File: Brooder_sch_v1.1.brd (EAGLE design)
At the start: 100 x 90 mm, 37 parts, among them J1 DCJ0202, J2 1X2-3.5MM, J3 DCJ0202, J4 1X2-3.5MM, T1 2N2222, U1 328P

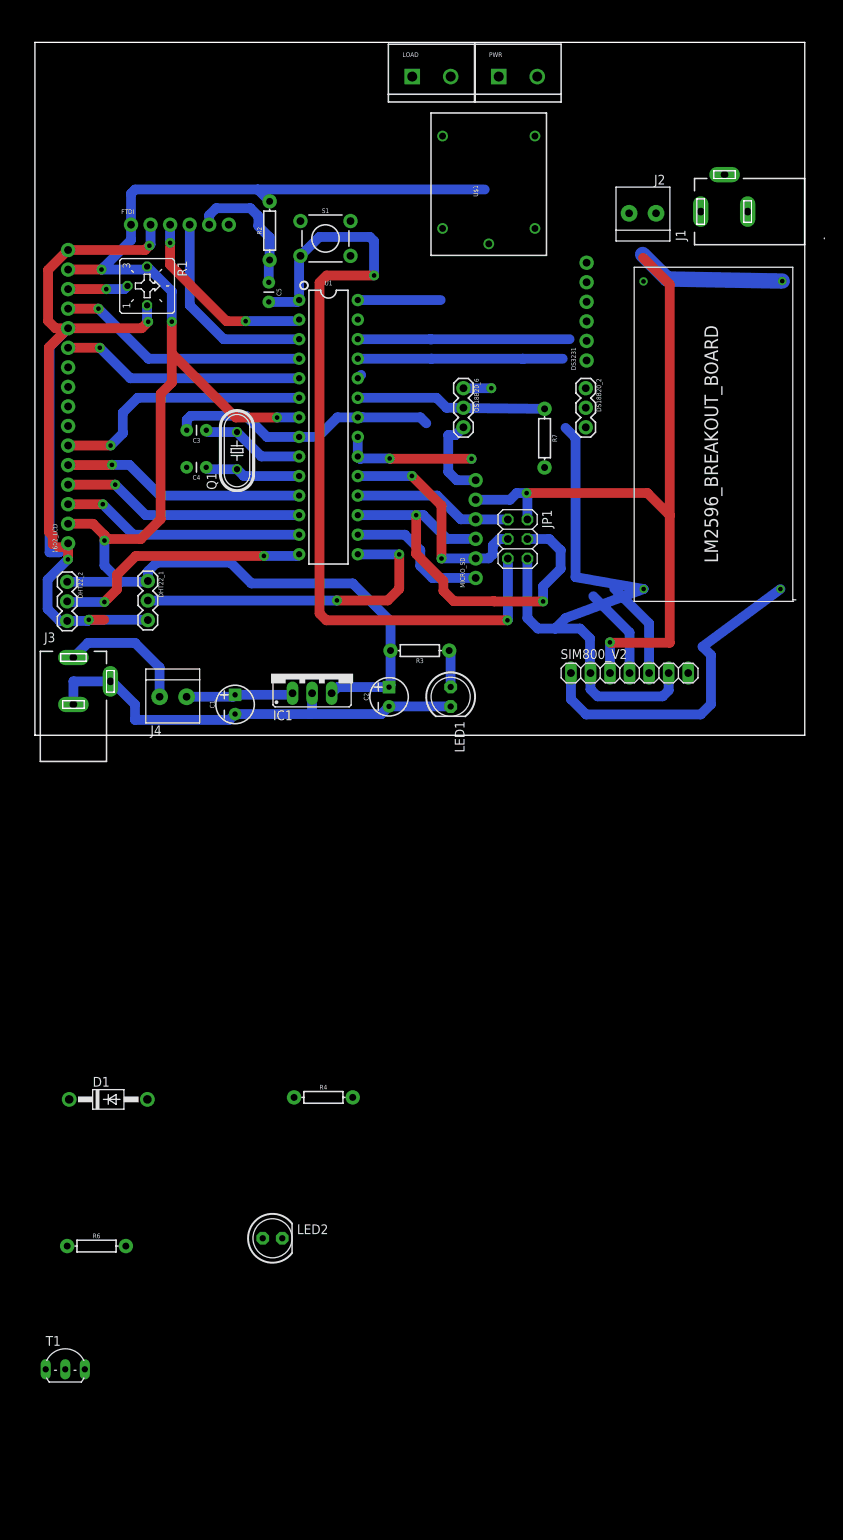
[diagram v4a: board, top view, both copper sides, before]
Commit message: Replaces both power jacks with header pins
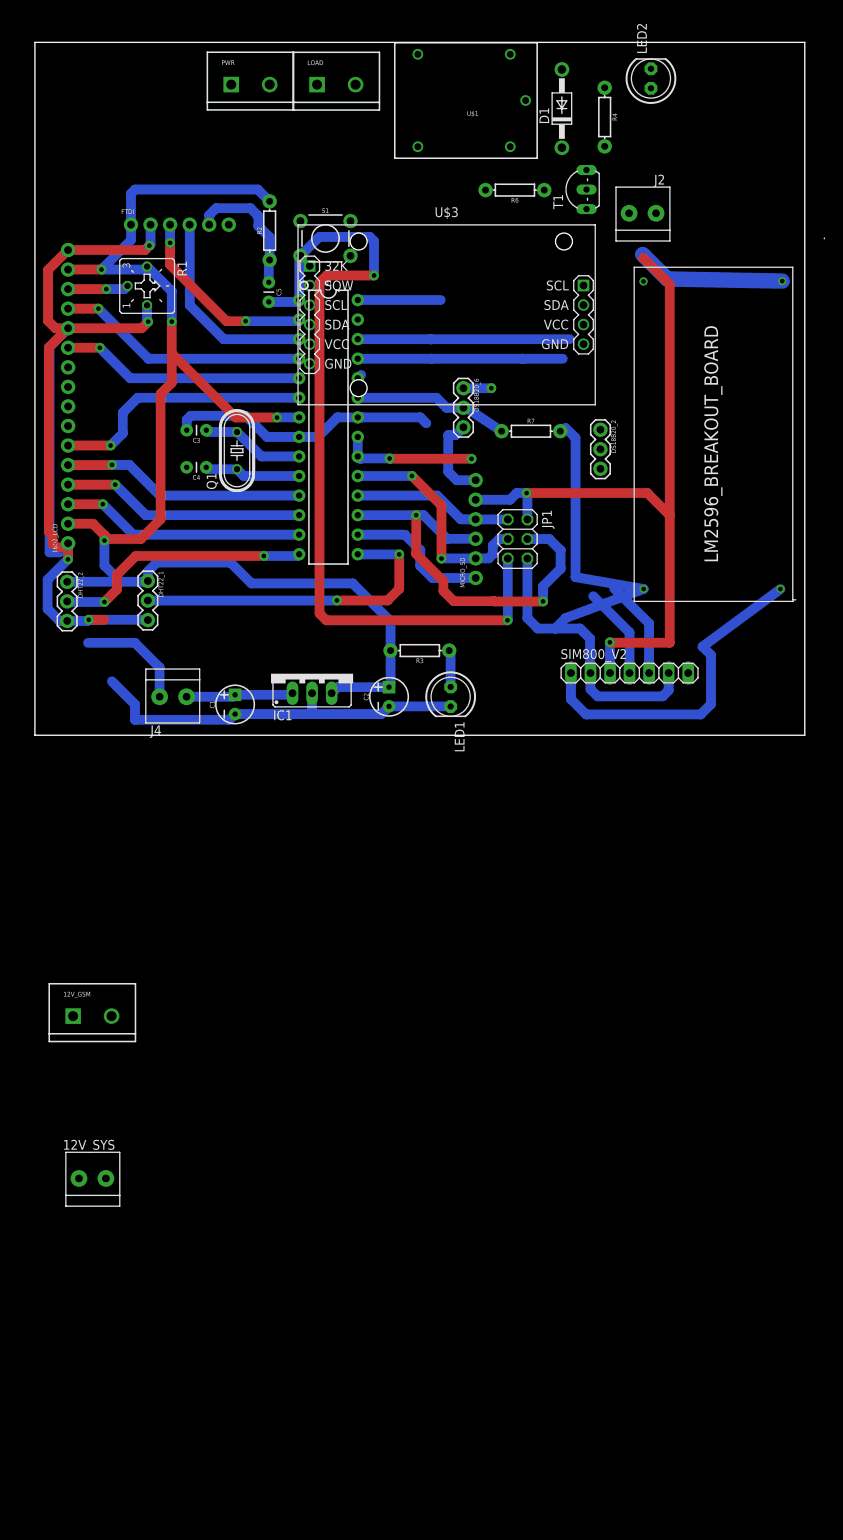
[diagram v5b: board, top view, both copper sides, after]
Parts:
- removed DS3231: (no value), SparkFun-Connectors:1X06_NO_SILK
- removed J1, J3: DCJ0202, con-jack:DCJ0202
- added 12V_GSM: (no value), SparkFun-Connectors:SCREWTERMINAL-5MM-2
- added 12V_SYS: 1X2-3.5MM, adafruit:1X2-3.5MM
- added U$3: RTC-DS3231-AT24C32, diy-modules-1.8.0:RTC-DS3231-AT24C32
- moved T1 165.9 mm to (70.4, 70.9), turned to 90 degrees
- moved LED2 158.5 mm to (80.0, 85.3), turned to 90 degrees
- moved R6 147.5 mm to (62.4, 70.8), turned to 180 degrees
- moved D1 141.5 mm to (68.5, 81.4), turned to 90 degrees
- moved R4 132.5 mm to (74.0, 80.3), turned to 270 degrees
- moved PWR 34.8 mm to (25.5, 84.5)
- moved LOAD 12.4 mm to (36.6, 84.5)
- moved U$1 11.4 mm to (56.4, 82.3), turned to 180 degrees
- moved DS18B20_2 5.72 mm to (73.5, 39.7)
- moved R7 1.99 mm to (64.4, 39.5), turned to 0 degrees
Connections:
- removed net PC4: DS3231.4, U1.27
- removed net PC5: DS3231.3, U1.28
- new net GND.1: U$3.J1.6
- new net SCL: U$3.J2.1, U1.28
- new net SDA: U$3.J2.2, U1.27
- new net VCC.1: U$3.J1.5
- net 12V: now also 12V_SYS.1; no longer J3.1
- net 12V_SIM: now also 12V_GSM.1; no longer J1.1
- net 5V: now also U$3.J2.3; no longer DS3231.5
- net GND: now also 12V_GSM.2, 12V_SYS.2, U$3.J2.4; no longer DS3231.6, J1.2, J1.3, J3.2, J3.3
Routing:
- net 5V: track 325.3 -> 295.8 mm
- net SCL: track 0.00 -> 10.8 mm
- net PC5: track 10.8 -> 0.00 mm
- net GND: track 313.0 -> 305.0 mm
- net PC0: track 24.8 -> 20.1 mm
- net 12V: track 17.1 -> 14.4 mm

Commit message: Adds custom sim800V2 library symbol to schematic
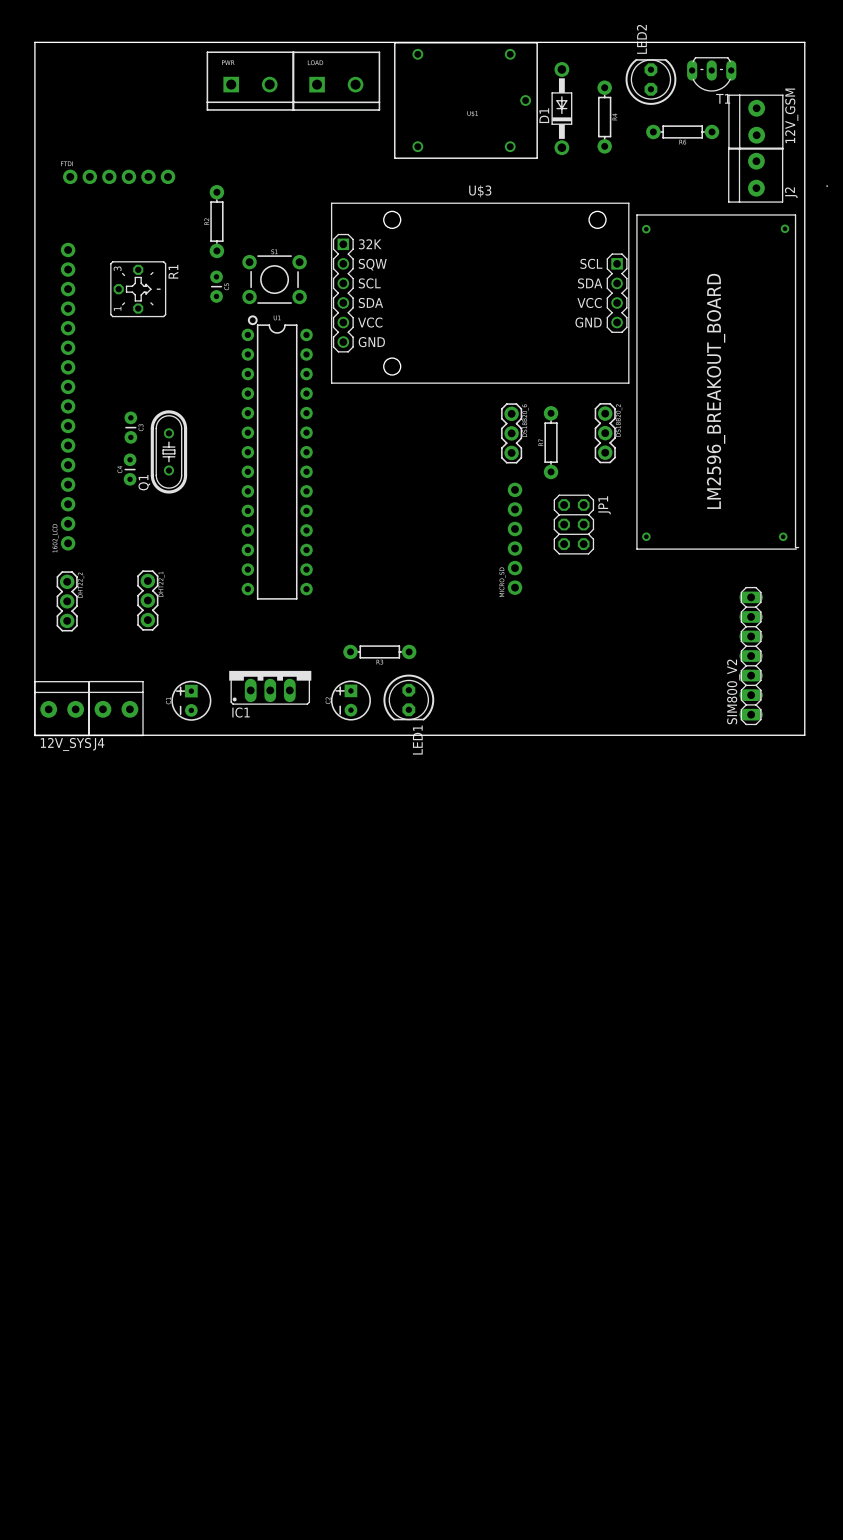
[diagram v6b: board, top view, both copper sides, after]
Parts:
- 12V_GSM: value (none) -> 1X2-3.5MM; device SparkFun-Connectors:SCREWTERMINAL-5MM-2 -> adafruit:1X2-3.5MM
- moved 12V_GSM 146.3 mm to (93.8, 79.7), turned to 270 degrees
- moved 12V_SYS 61.1 mm to (3.59, 3.36), turned to 180 degrees
- moved R6 23.1 mm to (84.1, 78.4)
- moved T1 22.6 mm to (87.9, 85.1), turned to 180 degrees
- moved SIM800_V2 15.9 mm to (93.0, 10.3), turned to 90 degrees
- moved J2 15.7 mm to (93.7, 72.9), turned to 270 degrees
- moved FTDI 10.0 mm to (4.59, 72.5)
- moved Q1 8.84 mm to (17.4, 36.8)
- moved C4 8.62 mm to (12.4, 34.5), turned to 90 degrees
- moved C3 8.54 mm to (12.5, 40.0), turned to 270 degrees
- moved S1 8.50 mm to (31.1, 59.2)
- moved U1 8.05 mm to (31.5, 35.5)
- moved JP1 7.55 mm to (70.0, 27.4)
- moved J4 7.54 mm to (10.6, 3.37)
- moved DS18B20_6 7.09 mm to (61.9, 41.8)
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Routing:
- net GND: track 305.0 -> 0.00 mm, vias 4 -> 0
- net 5V: track 295.8 -> 0.00 mm, vias 9 -> 0
- net RESET: track 108.6 -> 0.00 mm, vias 2 -> 0
- net MOSI: track 53.9 -> 0.00 mm, vias 2 -> 0
- net 5V_SIM: track 43.5 -> 0.00 mm
- net PB1: track 43.1 -> 0.00 mm, vias 2 -> 0
- net RX: track 40.5 -> 0.00 mm
- net TX: track 38.6 -> 0.00 mm
- net PD4: track 34.2 -> 0.00 mm, vias 1 -> 0
- net PB0: track 33.8 -> 0.00 mm, vias 2 -> 0
- net PD2: track 32.8 -> 0.00 mm, vias 1 -> 0
- net PD5: track 31.7 -> 0.00 mm, vias 1 -> 0
- net PD3: track 31.7 -> 0.00 mm, vias 1 -> 0
- net PD7: track 31.7 -> 0.00 mm, vias 1 -> 0
- net PD6: track 31.7 -> 0.00 mm, vias 1 -> 0
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
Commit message: Adds i2c header pin in place of lcd pins and potentiometer
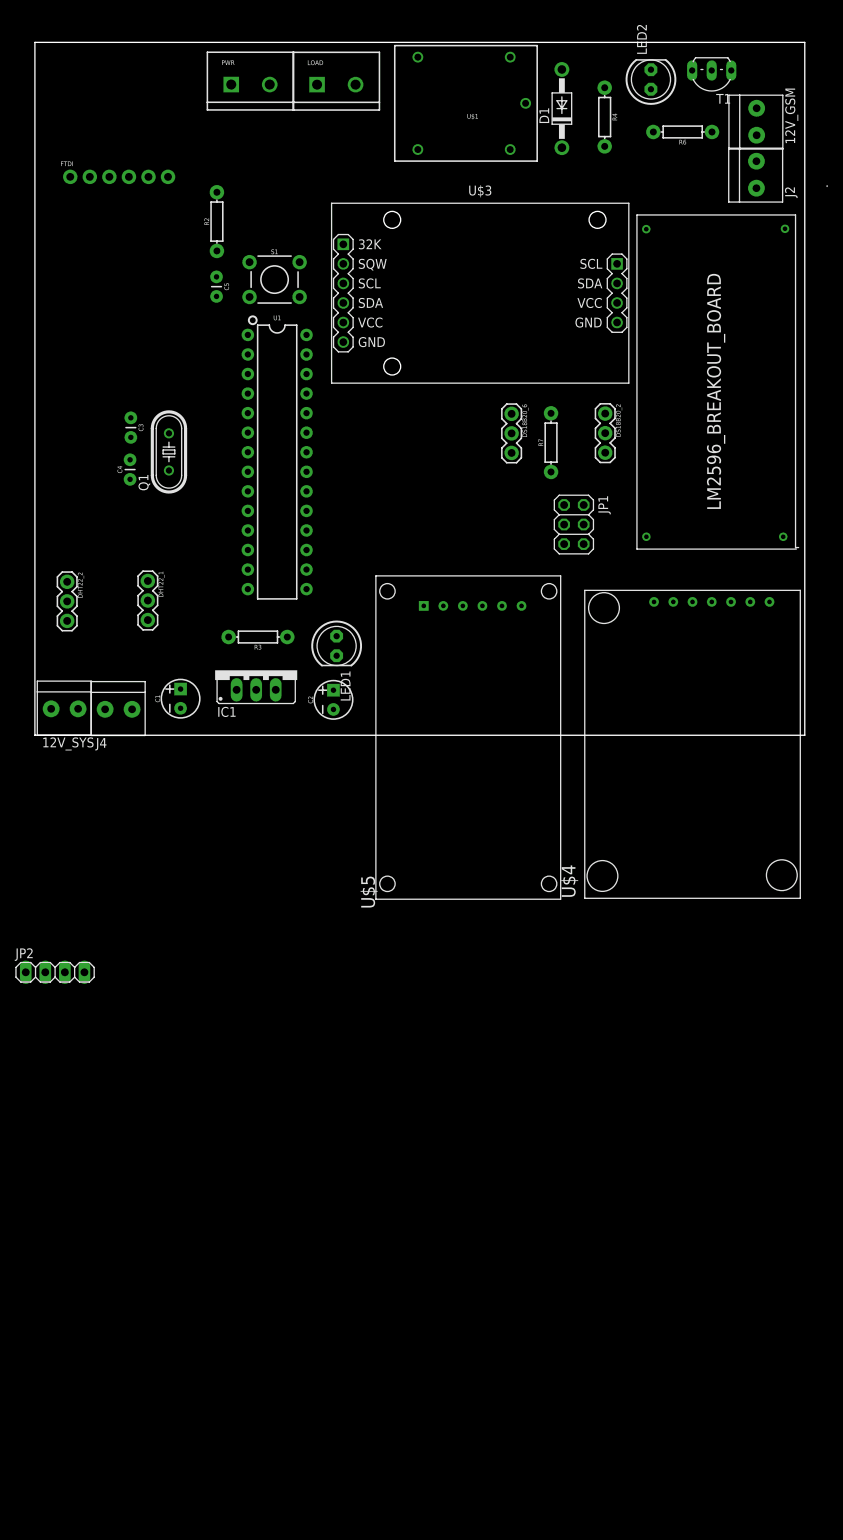
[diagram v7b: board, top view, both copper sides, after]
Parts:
- removed 1602_LCD: (no value), SparkFun-Connectors:1X16_NO_SILK
- removed MICRO_SD: (no value), SparkFun-Connectors:1X06_NO_SILK
- removed R1: (no value), pot:CT6
- removed SIM800_V2: (no value), pinhead:1X07
- added JP2: (no value), pinhead:1X04
- added U$4: (no value), custom_libraries:20*4_LCD
- added U$5: SD_CARD_MODULE, custom_libraries:SD_CARD_MODULE
- moved R3 15.9 mm to (29.0, 12.8)
- moved LED1 11.7 mm to (39.2, 11.6)
- moved C2 2.27 mm to (38.8, 4.60)
- moved IC1 1.83 mm to (28.7, 8.44)
- moved C1 1.43 mm to (18.9, 4.75)
- moved U$1 0.37 mm to (56.4, 82.0)
- moved 12V_SYS 0.33 mm to (3.91, 3.43)
- moved J4 0.28 mm to (10.9, 3.37)
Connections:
- removed net VO: 1602_LCD.14, R1.S
- net 5V: now also JP2.3, U$4.3, U$5.2; no longer 1602_LCD.15, 1602_LCD.2, MICRO_SD.5, R1.E, SIM800_V2.3
- net 5V_SIM: now also U$4.1; no longer SIM800_V2.1
- net GND: now also JP2.4, U$4.2, U$4.6, U$5.1; no longer 1602_LCD.1, 1602_LCD.12, 1602_LCD.16, MICRO_SD.6, R1.A, SIM800_V2.2, SIM800_V2.6
- net MISO: now also U$5.3; no longer MICRO_SD.4
- net MOSI: now also U$5.4; no longer MICRO_SD.3
- net PD2: no longer 1602_LCD.13
- net PD3: no longer 1602_LCD.11
- net PD4: no longer 1602_LCD.6
- net PD5: no longer 1602_LCD.5
- net PD6: no longer 1602_LCD.4
- net PD7: no longer 1602_LCD.3
- net RX: now also U$4.5; no longer SIM800_V2.5
- net SCK: now also U$5.5; no longer MICRO_SD.2
- net SCL: now also JP2.1
- net SDA: now also JP2.2
- net SS: now also U$5.6; no longer MICRO_SD.1
- net TX: now also U$4.4; no longer SIM800_V2.4

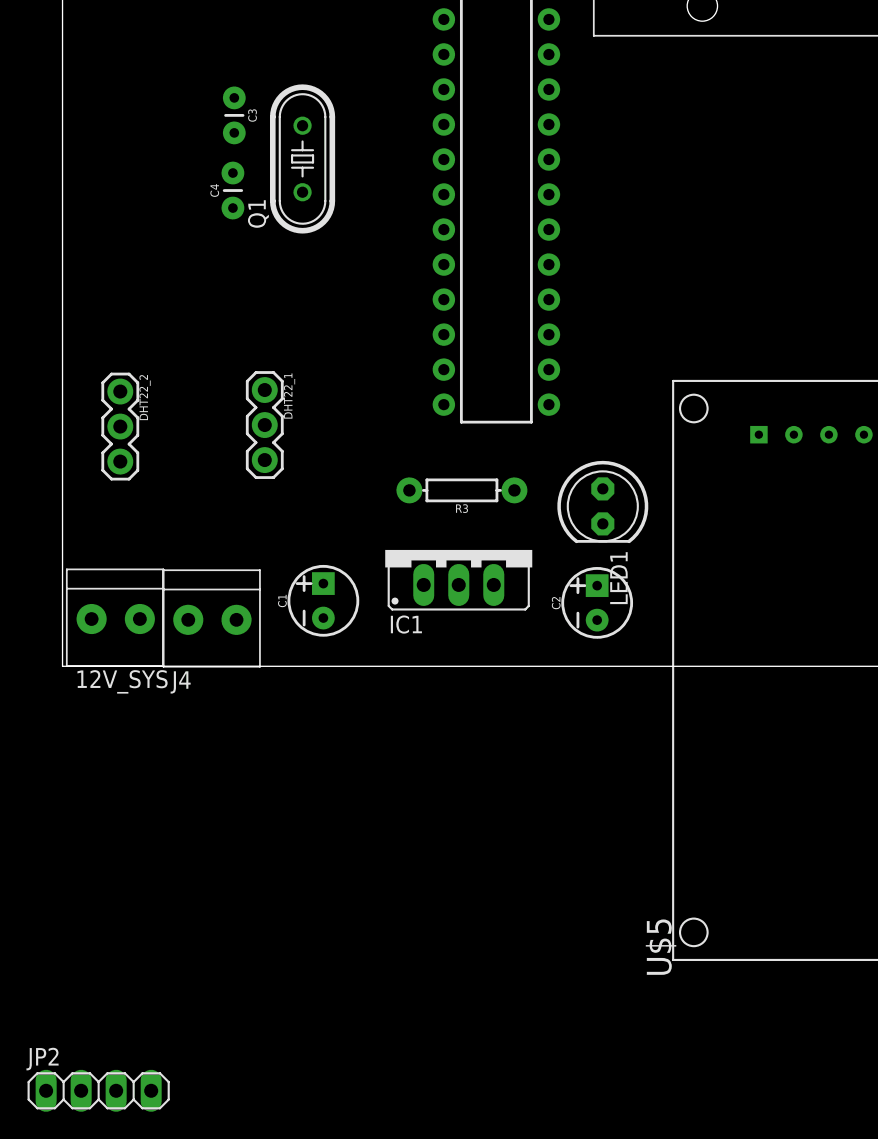
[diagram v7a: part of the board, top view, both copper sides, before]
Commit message: Removes extra ds18b20 pin
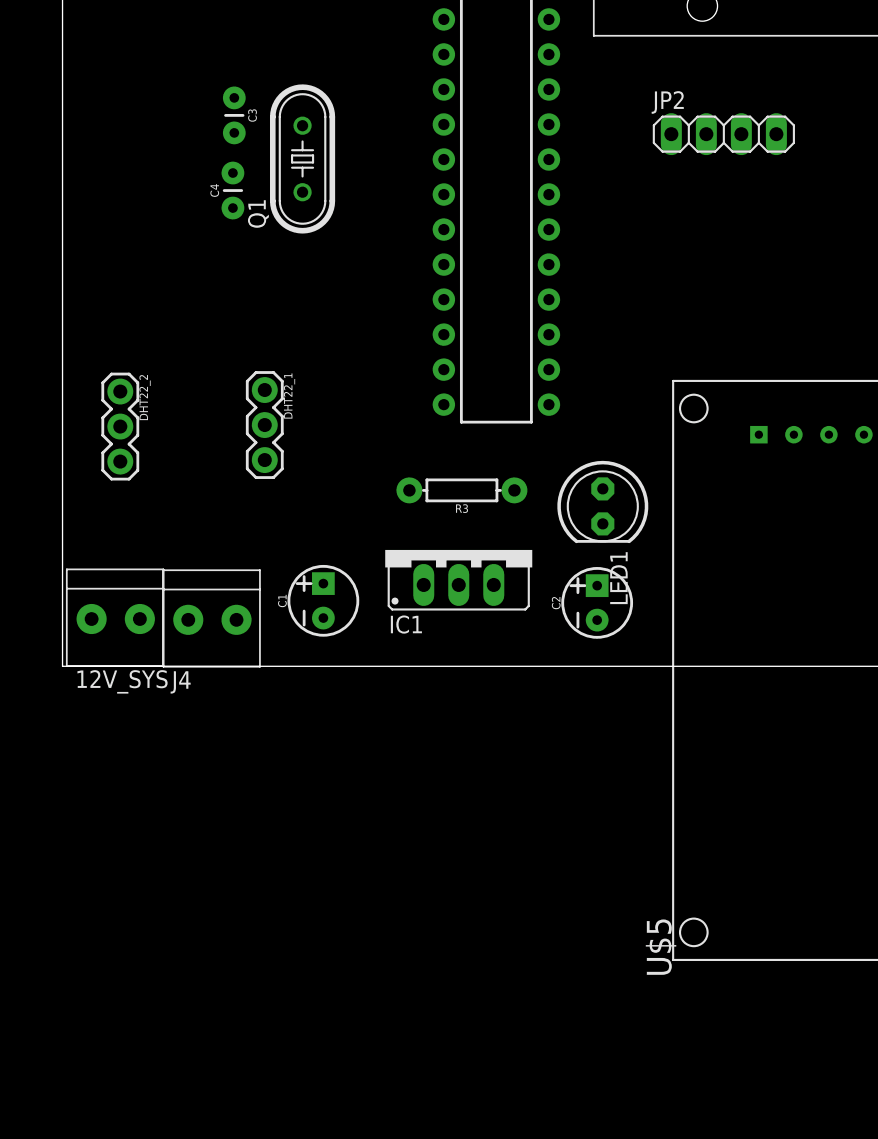
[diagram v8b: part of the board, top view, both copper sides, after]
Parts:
- moved JP2 82.9 mm to (48.0, 38.6)
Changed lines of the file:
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@@
 <element name="U$4" library="custom_libraries" package="20*4_LCD" value="" x="99.42" y="-21.18" rot="R90"/>
 <element name="U$5" library="custom_libraries" package="SD_CARD_MODULE" value="SD_CARD_MODULE" x="68.29" y="-21.3" rot="R90"/>
-<element name="JP2" library="pinhead" package="1X04" value="" x="2.62" y="-30.79"/>
+<element name="JP2" library="pinhead" package="1X04" value="" x="47.97" y="38.6"/>
 </elements>
 <signals>
@@
 <wire x1="27.8788" y1="61.4506" x2="35.28" y2="36.76" width="0" layer="19" extent="1-1"/>
 <wire x1="7.13" y1="72.53" x2="27.8788" y2="61.4506" width="0" layer="19" extent="1-1"/>
-<wire x1="6.43" y1="-30.79" x2="5.61" y2="3.43" width="0" layer="19" extent="1-1"/>
+<wire x1="51.78" y1="38.6" x2="5.61" y2="3.43" width="0" layer="19" extent="1-1"/>
 </signal>
 <signal name="12V">
@@
 <wire x1="23.64" y1="70.53" x2="27.66" y2="36.76" width="0" layer="19" extent="1-1"/>
 <wire x1="4.59" y1="72.53" x2="23.64" y2="70.53" width="0" layer="19" extent="1-1"/>
-<wire x1="3.89" y1="-30.79" x2="31.28" y2="5.9" width="0" layer="19" extent="1-1"/>
+<wire x1="49.24" y1="38.6" x2="31.28" y2="5.9" width="0" layer="19" extent="1-1"/>
 </signal>
 <signal name="N$5">
@@
 <contactref element="JP2" pad="1"/>
 <wire x1="35.28" y1="52" x2="75.62" y2="61.23" width="0" layer="19" extent="1-1"/>
-<wire x1="-1.19" y1="-30.79" x2="35.28" y2="52" width="0" layer="19" extent="1-1"/>
+<wire x1="44.16" y1="38.6" x2="35.28" y2="52" width="0" layer="19" extent="1-1"/>
 </signal>
 <signal name="SDA">
@@
 <contactref element="JP2" pad="2"/>
 <wire x1="35.28" y1="49.46" x2="75.62" y2="58.69" width="0" layer="19" extent="1-1"/>
-<wire x1="1.35" y1="-30.79" x2="35.28" y2="49.46" width="0" layer="19" extent="1-1"/>
+<wire x1="46.7" y1="38.6" x2="35.28" y2="49.46" width="0" layer="19" extent="1-1"/>
 </signal>
 </signals>
